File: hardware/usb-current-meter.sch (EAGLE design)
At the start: 30 parts, among them IC2 LM358, U1 ATTINY45, X1 MC2, X3 USB-A-H

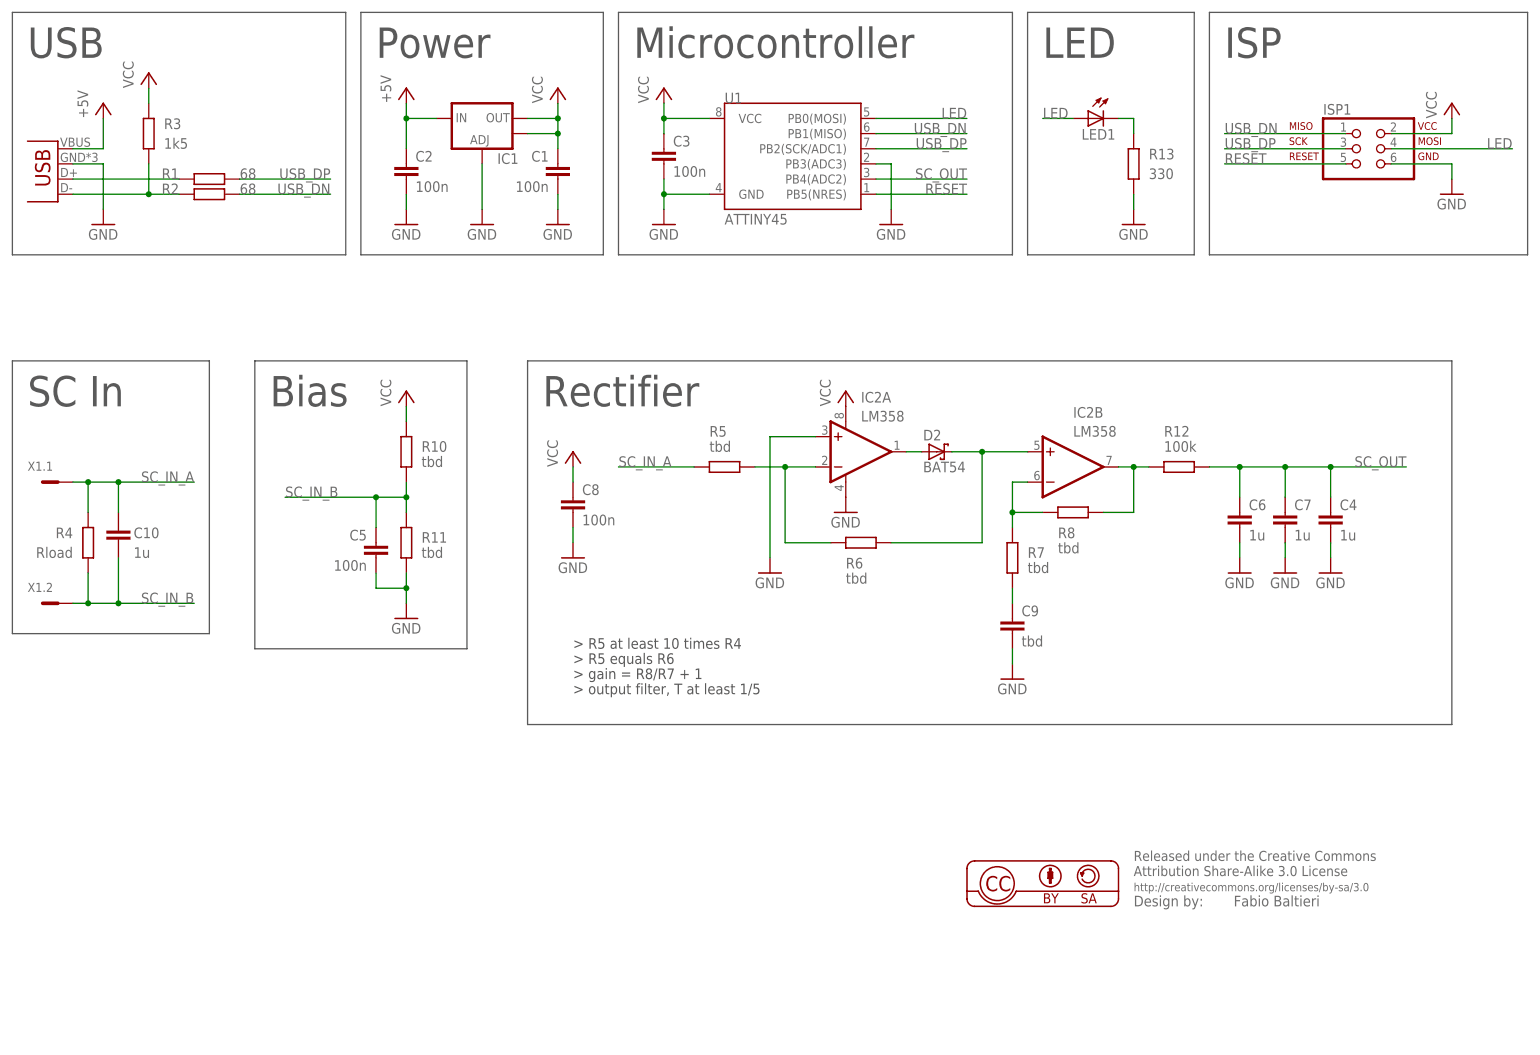
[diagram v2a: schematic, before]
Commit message: hardware: update variants, add notes
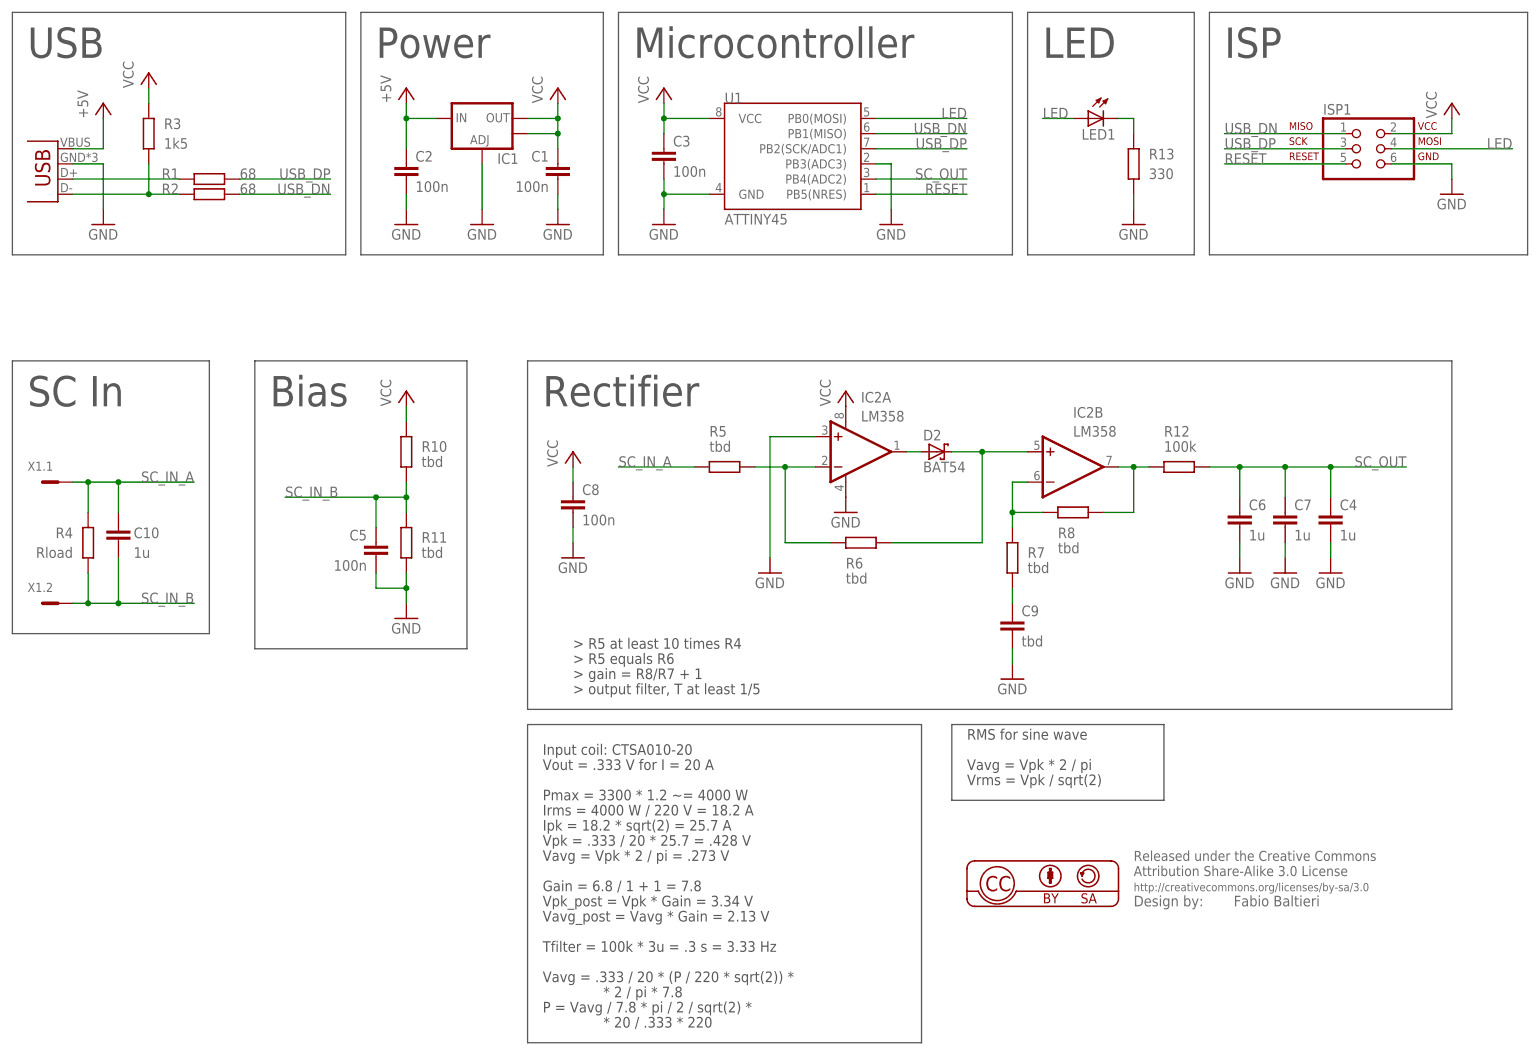
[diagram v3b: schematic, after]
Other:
- note added: "* 2 / pi * 7.8"
- note added: "* 20 / .333 * 220"
- note added: "Gain = 6.8 / 1 + 1 = 7.8"
- note added: "Input coil: CTSA010-20"
- note added: "Ipk = 18.2 * sqrt(2) = 25.7 A"
- note added: "Irms = 4000 W / 220 V = 18.2 A"
- note added: "P = Vavg / 7.8 * pi / 2 / sqrt(2) *"
- note added: "Pmax = 3300 * 1.2 ~= 4000 W"
- note added: "RMS for sine wave"
- note added: "Tfilter = 100k * 3u = .3 s = 3.33 Hz"
- note added: "Vavg = .333 / 20 * (P / 220 * sqrt(2)) *"
- note added: "Vavg = Vpk * 2 / pi"
- note added: "Vavg = Vpk * 2 / pi = .273 V"
- note added: "Vavg_post = Vavg * Gain = 2.13 V"
- note added: "Vout = .333 V for I = 20 A"
- note added: "Vpk = .333 / 20 * 25.7 = .428 V"
- note added: "Vpk_post = Vpk * Gain = 3.34 V"
- note added: "Vrms = Vpk / sqrt(2)"
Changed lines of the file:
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@@
 <part name="R5" library="rcl" deviceset="R-EU_" device="R0603" value="tbd">
 <variant name="bias" value="0"/>
+<variant name="rectifier" value="10k"/>
 </part>
 <part name="R6" library="rcl" deviceset="R-EU_" device="R0603" value="tbd">
 <variant name="bias" value="0"/>
+<variant name="rectifier" value="10k"/>
 </part>
 <part name="GND6" library="supply1" deviceset="GND" device=""/>
@@
 <part name="R7" library="rcl" deviceset="R-EU_" device="R0603" value="tbd">
 <variant name="bias" populate="no"/>
+<variant name="rectifier" value="1k"/>
 </part>
 <part name="R8" library="rcl" deviceset="R-EU_" device="R0603" value="tbd">
 <variant name="bias" populate="no"/>
+<variant name="rectifier" value="6.8k"/>
 </part>
 <part name="GND8" library="supply1" deviceset="GND" device=""/>
@@
 <part name="GND10" library="supply1" deviceset="GND" device=""/>
 <part name="LICENSE1" library="balto" deviceset="CC_BY-SA" device="" value="Fabio Baltieri"/>
-<part name="C9" library="rcl" deviceset="C-EU" device="C0805" value="tbd"/>
+<part name="C9" library="rcl" deviceset="C-EU" device="C0805" value="tbd">
+<variant name="rectifier" value="0"/>
+</part>
 <part name="C10" library="rcl" deviceset="C-EU" device="C0805" value="1u"/>
 </parts>
@@
 <wire x1="175.26" y1="134.62" x2="175.26" y2="175.26" width="0.1524" layer="97"/>
 <wire x1="246.38" y1="116.84" x2="91.44" y2="116.84" width="0.1524" layer="97"/>
-<wire x1="91.44" y1="116.84" x2="91.44" y2="55.88" width="0.1524" layer="97"/>
-<wire x1="91.44" y1="55.88" x2="246.38" y2="55.88" width="0.1524" layer="97"/>
-<wire x1="246.38" y1="55.88" x2="246.38" y2="116.84" width="0.1524" layer="97"/>
+<wire x1="91.44" y1="116.84" x2="91.44" y2="58.42" width="0.1524" layer="97"/>
+<wire x1="91.44" y1="58.42" x2="246.38" y2="58.42" width="0.1524" layer="97"/>
+<wire x1="246.38" y1="58.42" x2="246.38" y2="116.84" width="0.1524" layer="97"/>
 <wire x1="45.72" y1="116.84" x2="81.28" y2="116.84" width="0.1524" layer="97"/>
 <wire x1="81.28" y1="116.84" x2="81.28" y2="68.58" width="0.1524" layer="97"/>
@@
 <text x="99.06" y="63.5" size="1.778" layer="97">&gt; gain = R8/R7 + 1</text>
 <text x="99.06" y="60.96" size="1.778" layer="97">&gt; output filter, T at least 1/5</text>
+<text x="93.98" y="43.18" size="1.778" layer="97">Pmax = 3300 * 1.2 ~= 4000 W</text>
+<text x="93.98" y="40.64" size="1.778" layer="97">Irms = 4000 W / 220 V = 18.2 A</text>
+<text x="93.98" y="38.1" size="1.778" layer="97">Ipk = 18.2 * sqrt(2) = 25.7 A</text>
+<text x="93.98" y="35.56" size="1.778" layer="97">Vpk = .333 / 20 * 25.7 = .428 V</text>
+<text x="93.98" y="48.26" size="1.778" layer="97">Vout = .333 V for I = 20 A</text>
+<text x="93.98" y="50.8" size="1.778" layer="97">Input coil: CTSA010-20</text>
+<text x="93.98" y="33.02" size="1.778" layer="97">Vavg = Vpk * 2 / pi = .273 V</text>
+<text x="93.98" y="27.94" size="1.778" layer="97">Gain = 6.8 / 1 + 1 = 7.8</text>
+<text x="93.98" y="25.4" size="1.778" layer="97">Vpk_post = Vpk * Gain = 3.34 V</text>
+<text x="93.98" y="22.86" size="1.778" layer="97">Vavg_post = Vavg * Gain = 2.13 V</text>
+<text x="165.1" y="53.34" size="1.778" layer="97">RMS for sine wave</text>
+<text x="165.1" y="48.26" size="1.778" layer="97">Vavg = Vpk * 2 / pi</text>
+<text x="165.1" y="45.72" size="1.778" layer="97">Vrms = Vpk / sqrt(2)</text>
+<wire x1="91.44" y1="55.88" x2="157.48" y2="55.88" width="0.1524" layer="97"/>
+<wire x1="157.48" y1="55.88" x2="157.48" y2="2.54" width="0.1524" layer="97"/>
+<wire x1="157.48" y1="2.54" x2="91.44" y2="2.54" width="0.1524" layer="97"/>
+<wire x1="91.44" y1="2.54" x2="91.44" y2="55.88" width="0.1524" layer="97"/>
+<wire x1="162.56" y1="55.88" x2="198.12" y2="55.88" width="0.1524" layer="97"/>
+<wire x1="198.12" y1="55.88" x2="198.12" y2="43.18" width="0.1524" layer="97"/>
+<wire x1="198.12" y1="43.18" x2="162.56" y2="43.18" width="0.1524" layer="97"/>
+<wire x1="162.56" y1="43.18" x2="162.56" y2="55.88" width="0.1524" layer="97"/>
+<text x="93.98" y="17.78" size="1.778" layer="97">Tfilter = 100k * 3u = .3 s = 3.33 Hz</text>
+<text x="93.98" y="12.7" size="1.778" layer="97">Vavg = .333 / 20 * (P / 220 * sqrt(2)) *</text>
+<text x="104.14" y="10.16" size="1.778" layer="97">* 2 / pi * 7.8</text>
+<text x="93.98" y="7.62" size="1.778" layer="97">P = Vavg / 7.8 * pi / 2 / sqrt(2) *</text>
+<text x="104.14" y="5.08" size="1.778" layer="97">* 20 / .333 * 220</text>
 </plain>
 <instances>

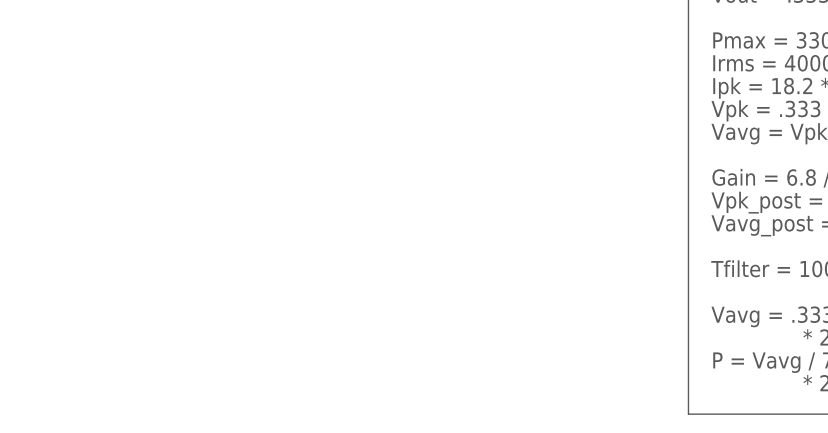
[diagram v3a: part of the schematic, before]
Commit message: hardware: add calculations for 6.5kW full-scale
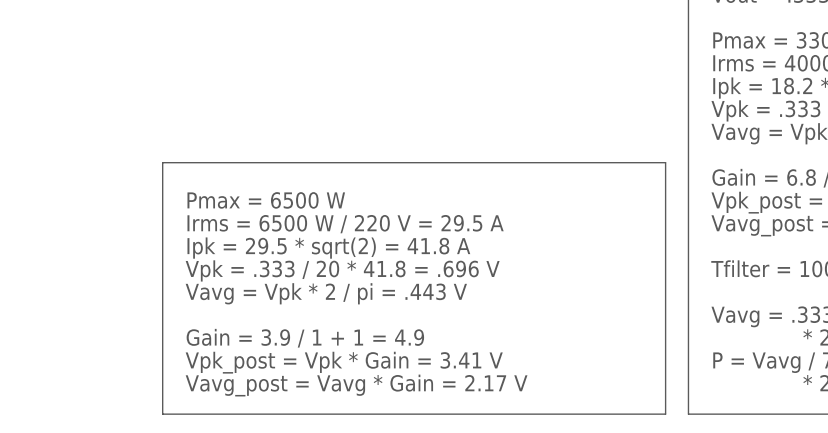
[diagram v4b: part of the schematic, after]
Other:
- note added: "Gain = 3.9 / 1 + 1 = 4.9"
- note added: "Ipk = 29.5 * sqrt(2) = 41.8 A"
- note added: "Irms = 6500 W / 220 V = 29.5 A"
- note added: "Pmax = 6500 W"
- note added: "Vavg = Vpk * 2 / pi = .443 V"
- note added: "Vavg_post = Vavg * Gain = 2.17 V"
- note added: "Vpk = .333 / 20 * 41.8 = .696 V"
- note added: "Vpk_post = Vpk * Gain = 3.41 V"
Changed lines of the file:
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@@
 <text x="93.98" y="7.62" size="1.778" layer="97">P = Vavg / 7.8 * pi / 2 / sqrt(2) *</text>
 <text x="104.14" y="5.08" size="1.778" layer="97">* 20 / .333 * 220</text>
+<text x="35.56" y="25.4" size="1.778" layer="97">Pmax = 6500 W</text>
+<text x="35.56" y="22.86" size="1.778" layer="97">Irms = 6500 W / 220 V = 29.5 A</text>
+<text x="35.56" y="20.32" size="1.778" layer="97">Ipk = 29.5 * sqrt(2) = 41.8 A</text>
+<text x="35.56" y="17.78" size="1.778" layer="97">Vpk = .333 / 20 * 41.8 = .696 V</text>
+<text x="35.56" y="15.24" size="1.778" layer="97">Vavg = Vpk * 2 / pi = .443 V</text>
+<text x="35.56" y="10.16" size="1.778" layer="97">Gain = 3.9 / 1 + 1 = 4.9</text>
+<text x="35.56" y="7.62" size="1.778" layer="97">Vpk_post = Vpk * Gain = 3.41 V</text>
+<text x="35.56" y="5.08" size="1.778" layer="97">Vavg_post = Vavg * Gain = 2.17 V</text>
+<wire x1="33.02" y1="30.48" x2="88.9" y2="30.48" width="0.1524" layer="97"/>
+<wire x1="88.9" y1="30.48" x2="88.9" y2="2.54" width="0.1524" layer="97"/>
+<wire x1="88.9" y1="2.54" x2="33.02" y2="2.54" width="0.1524" layer="97"/>
+<wire x1="33.02" y1="2.54" x2="33.02" y2="30.48" width="0.1524" layer="97"/>
 </plain>
 <instances>
